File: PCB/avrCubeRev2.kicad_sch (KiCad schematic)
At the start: 24 parts, among them J2 Conn_01x06_Male, SW1 SW_Push, U1 ATtiny24-20PU, U2 MMA8653FCR1

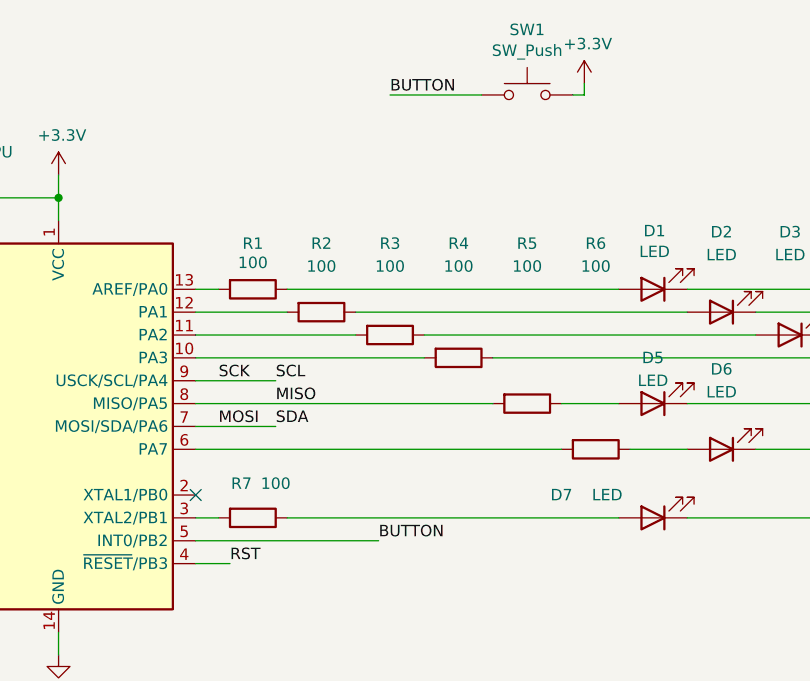
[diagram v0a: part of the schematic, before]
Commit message: Exported Gerber, Added Comments, Added Doxygen
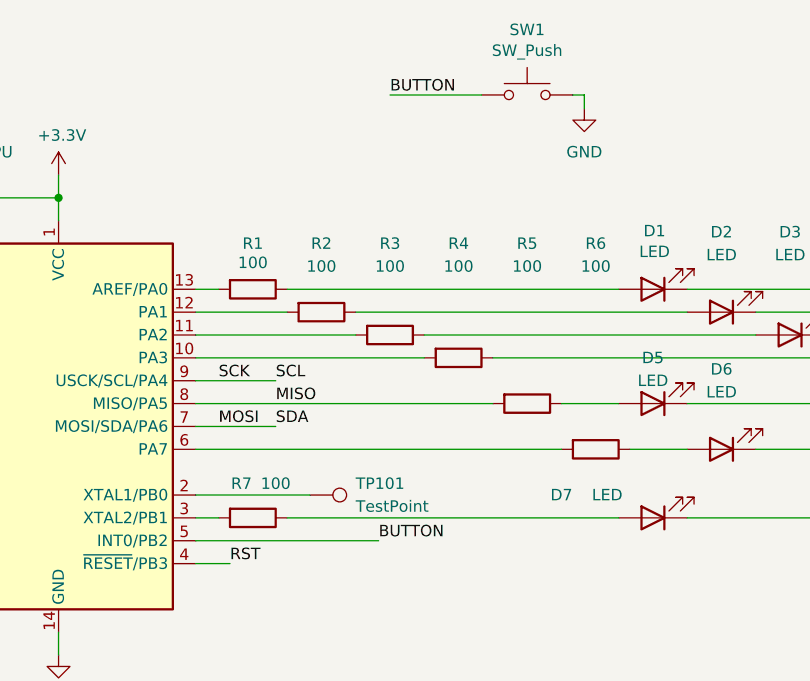
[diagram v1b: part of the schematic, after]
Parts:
- added TP101: TestPoint, TestPoint:TestPoint_2Pads_Pitch2.54mm_Drill0.8mm, symbol Connector:TestPoint
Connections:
- net +3V3: no longer SW1.2
- net GND: now also SW1.2
- net at U1.2 (XTAL1/PB0): now also TP101.1
- no-connect marks 3 -> 2
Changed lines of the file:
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@@
   (no_connect (at 120.65 153.67))
   (no_connect (at 120.65 151.13))
-  (no_connect (at 125.73 104.14))
   (wire (pts (xy 158.75 144.78) (xy 175.26 144.78))
     (stroke (width 0) (type default) (color 0 0 0 0))
@@
     (stroke (width 0) (type default) (color 0 0 0 0))
   )
+  (wire (pts (xy 125.73 104.14) (xy 138.43 104.14))
+    (stroke (width 0) (type default) (color 0 0 0 0))
+  )
   (wire (pts (xy 125.73 93.98) (xy 158.75 93.98))
     (stroke (width 0) (type default) (color 0 0 0 0))
@@
     (stroke (width 0) (type default) (color 0 0 0 0))
   )
-  (wire (pts (xy 168.91 58.42) (xy 168.91 59.69))
-    (stroke (width 0) (type default) (color 0 0 0 0))
-  )
   (wire (pts (xy 105.41 163.83) (xy 107.95 163.83))
     (stroke (width 0) (type default) (color 0 0 0 0))
@@
   )
   (wire (pts (xy 180.34 93.98) (xy 205.74 93.98))
+    (stroke (width 0) (type default) (color 0 0 0 0))
+  )
+  (wire (pts (xy 168.91 59.69) (xy 168.91 61.214))
     (stroke (width 0) (type default) (color 0 0 0 0))
   )
@@
     (pin "6")
   )
-  (symbol (lib_id "power:+3.3V") (at 168.91 58.42 0) (unit 1)
-    (in_bom yes) (on_board yes)
-    (property "Reference" "#PWR?" (id 0) (at 168.91 62.23 0)
-      (effects (font (size 1.27 1.27)) hide)
-    )
-    (property "Value" "+3.3V" (id 1) (at 169.291 54.0258 0))
-    (property "Footprint" "" (id 2) (at 168.91 58.42 0)
-      (effects (font (size 1.27 1.27)) hide)
-    )
-    (property "Datasheet" "" (id 3) (at 168.91 58.42 0)
+  (symbol (lib_id "Connector:TestPoint") (at 138.43 104.14 270) (unit 1)
+    (in_bom yes) (on_board yes) (fields_autoplaced)
+    (property "Reference" "TP101" (id 0) (at 143.51 102.8699 90)
+      (effects (font (size 1.27 1.27)) (justify left))
+    )
+    (property "Value" "TestPoint" (id 1) (at 143.51 105.4099 90)
+      (effects (font (size 1.27 1.27)) (justify left))
+    )
+    (property "Footprint" "TestPoint:TestPoint_2Pads_Pitch2.54mm_Drill0.8mm" (id 2) (at 138.43 109.22 0)
+      (effects (font (size 1.27 1.27)) hide)
+    )
+    (property "Datasheet" "~" (id 3) (at 138.43 109.22 0)
+      (effects (font (size 1.27 1.27)) hide)
+    )
+    (pin "1")
+  )
+  (symbol (lib_id "power:GND") (at 168.91 61.214 0) (unit 1)
+    (in_bom yes) (on_board yes) (fields_autoplaced)
+    (property "Reference" "#PWR0101" (id 0) (at 168.91 67.564 0)
+      (effects (font (size 1.27 1.27)) hide)
+    )
+    (property "Value" "GND" (id 1) (at 168.91 66.04 0))
+    (property "Footprint" "" (id 2) (at 168.91 61.214 0)
+      (effects (font (size 1.27 1.27)) hide)
+    )
+    (property "Datasheet" "" (id 3) (at 168.91 61.214 0)
       (effects (font (size 1.27 1.27)) hide)
     )
@@
       (reference "#PWR015") (unit 1) (value "GND") (footprint "")
     )
-    (path "/3f27385f-cbe1-45c9-ac9a-1c2672a2a35d"
-      (reference "#PWR?") (unit 1) (value "+3.3V") (footprint "")
+    (path "/9421d8ab-ec24-4783-b746-a12fbd00100e"
+      (reference "#PWR0101") (unit 1) (value "GND") (footprint "")
     )
     (path "/00000000-0000-0000-0000-000060ad77ae"
@@
       (reference "SW1") (unit 1) (value "SW_Push") (footprint "Buttons_Switches_THT:SW_PUSH_6mm_h4.3mm")
     )
+    (path "/1c22b557-5a80-4779-b5bc-44503ba180ce"
+      (reference "TP101") (unit 1) (value "TestPoint") (footprint "TestPoint:TestPoint_2Pads_Pitch2.54mm_Drill0.8mm")
+    )
     (path "/00000000-0000-0000-0000-000060b0e42f"
